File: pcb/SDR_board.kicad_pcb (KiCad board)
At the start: 4 copper layers, 100 x 100 mm, 469 parts, among them J1 USB_B_Mini, J201 Molex 73251-1150 SMA, J301 Molex 73251-1150 SMA, J401 Molex 73251-1150 SMA, J501 Molex 73251-1150 SMA, SW1 SW_Push, U1 AMS1117-3.3, U2 NB3L553, U201 BGA2803, U202 MSi001-Q40, U203 MAX19777AZA+, U204 ADS7883, U205 LMV712-N, U206 MAX19777AZA+, U207 ADS7883, U3 CY7C68013A-56PVX, U301 BGA2803, U302 MSi001-Q40, U303 MAX19777AZA+, U304 ADS7883, U305 LMV712-N, U306 MAX19777AZA+, U307 ADS7883, U401 BGA2803, U402 MSi001-Q40, U403 MAX19777AZA+, U404 ADS7883, U405 LMV712-N, U406 MAX19777AZA+, U407 ADS7883, U5 24LC128, U501 BGA2803, U502 MSi001-Q40, U503 MAX19777AZA+, U504 ADS7883, U505 LMV712-N, U506 MAX19777AZA+, U507 ADS7883, U6 MCP1825S, X1 XO32, X2 XO32

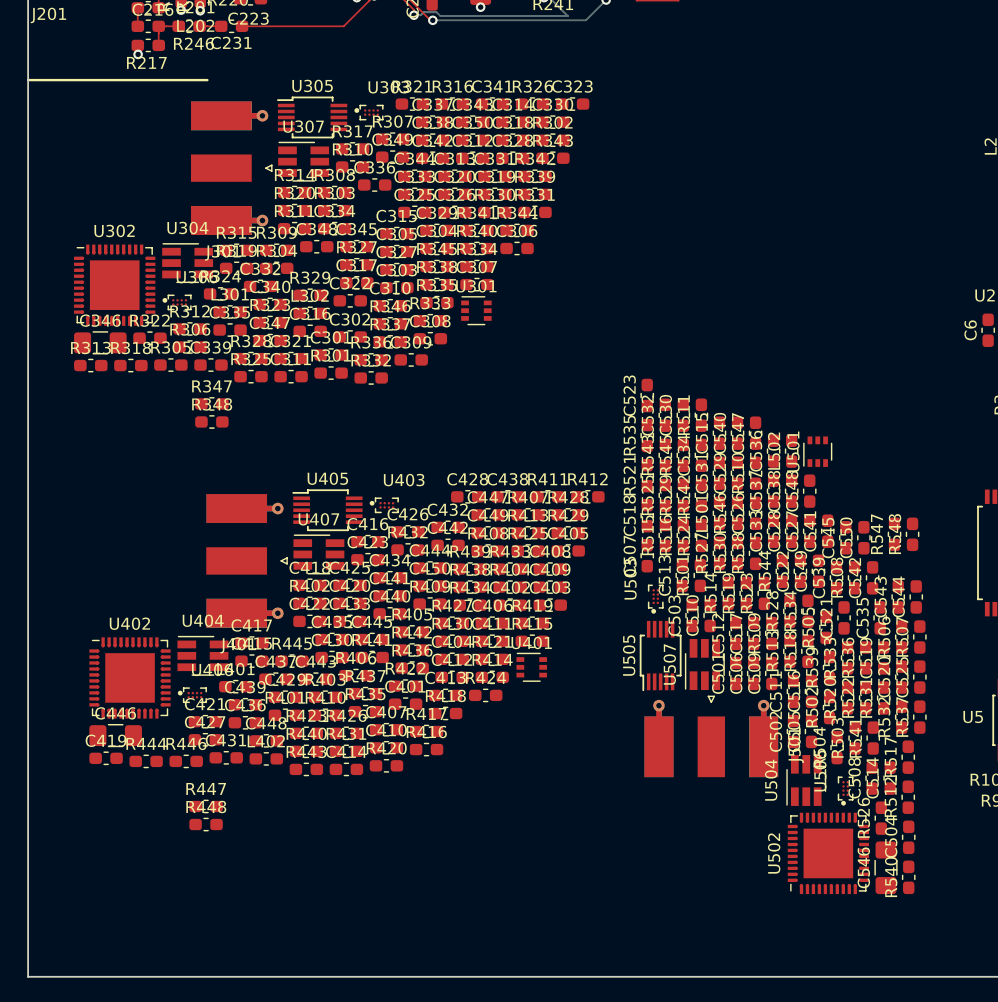
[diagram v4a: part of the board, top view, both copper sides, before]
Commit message: Duplicated the layouts for the other channels successfully using an old version of MitjaNemec/Kicad_action_plugins
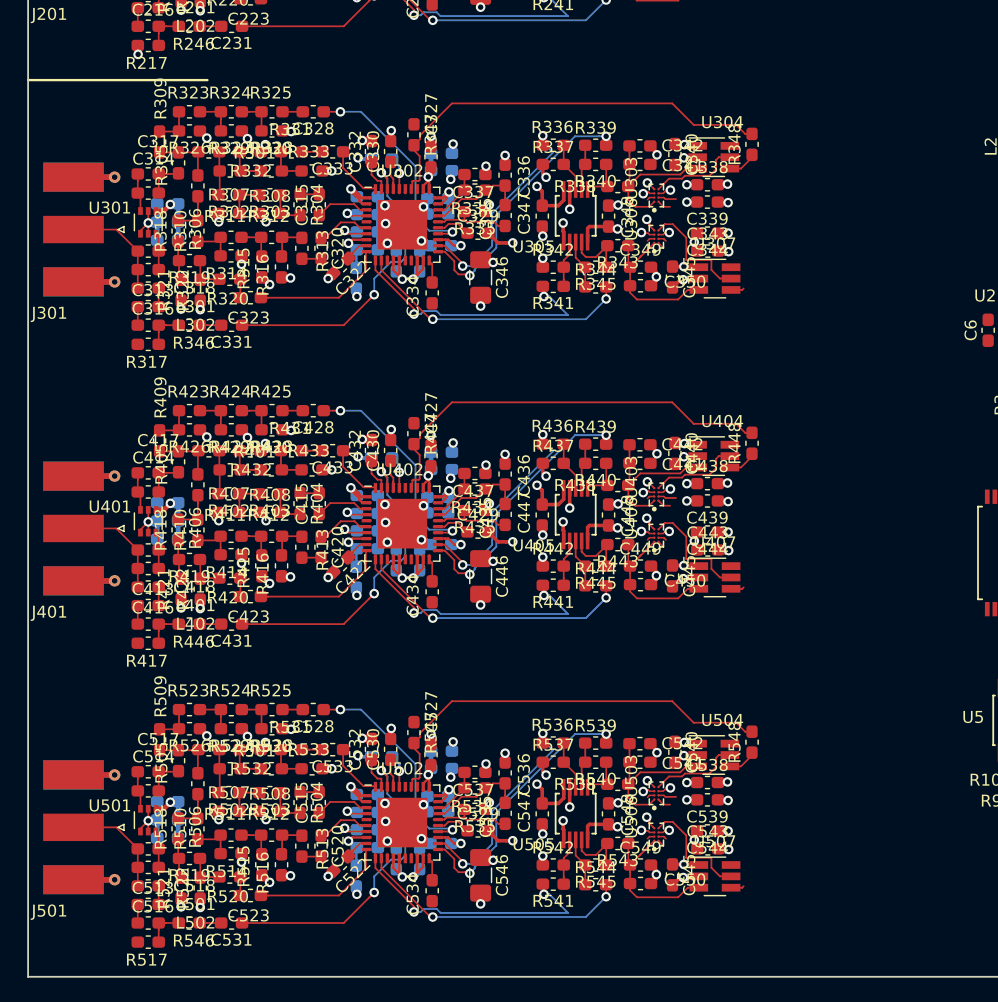
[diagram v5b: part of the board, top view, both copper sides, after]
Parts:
- C301, C302, C303, C304, C305, C306, C307, C308, C309, C310, C311, C312, C319, C321, C325, C326, C401, C402, C403, C404, C405, C406, C407, C408, C409, C410, C411, C412, C419, C421, C425, C426, C501, C502, C503, C504, C505, C506, C507, C508, C509, C510, C511, C512, C519, C521, C525, C526: moved to B.Cu
- moved L502 66.7 mm to (35.0, 115.5), turned to 0 degrees
- moved R517 65.4 mm to (35.0, 117.1), turned to 180 degrees
- moved U501 63.9 mm to (35.0, 106.9), turned to 270 degrees
- moved C514 62.1 mm to (35.0, 104.5), turned to 180 degrees
- moved R506 60.1 mm to (39.2, 103.8)
- moved R507 59.6 mm to (41.8, 106.2), turned to 0 degrees
- moved R526 58.3 mm to (38.5, 99.3), turned to 180 degrees
- moved L501 57.9 mm to (35.0, 114.0), turned to 180 degrees
- moved R522 57.9 mm to (39.4, 112.6)
- moved C516 57.4 mm to (35.0, 110.8), turned to 180 degrees
- moved R546 57.3 mm to (38.5, 115.5), turned to 180 degrees
- moved R448 55.7 mm to (85.5, 75.4), turned to 90 degrees
- moved C531 55.5 mm to (42.0, 115.5), turned to 180 degrees
- moved R510 55.3 mm to (39.2, 107.6)
- moved R505 55.3 mm to (37.6, 101.9), turned to 270 degrees
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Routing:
- net GND: track 80.2 -> 318.5 mm, vias 49 -> 193
- net +3.3VA: track 50.5 -> 201.8 mm, vias 19 -> 76
- net Net-(R547-Pad2): track 0.00 -> 35.3 mm
- net Net-(R447-Pad2): track 0.00 -> 35.3 mm
- net Net-(R347-Pad2): track 0.00 -> 35.3 mm
- net Net-(C331-Pad1): track 0.00 -> 26.4 mm, vias 0 -> 2
- net Net-(C531-Pad1): track 0.00 -> 26.4 mm, vias 0 -> 2
- net Net-(C431-Pad1): track 0.00 -> 26.4 mm, vias 0 -> 2
- net /Channel 4/I_N: track 0.00 -> 23.0 mm, vias 0 -> 2
- net /Channel 3/I_N: track 0.00 -> 23.0 mm, vias 0 -> 2
- net /Channel 2/I_N: track 0.00 -> 23.0 mm, vias 0 -> 2
- net /Channel 4/I_P: track 0.00 -> 22.4 mm, vias 0 -> 2
- net /Channel 3/I_P: track 0.00 -> 22.4 mm, vias 0 -> 2
- net /Channel 2/I_P: track 0.00 -> 22.4 mm, vias 0 -> 2
- net /Channel 4/Q_N: track 0.00 -> 21.8 mm, vias 0 -> 2
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
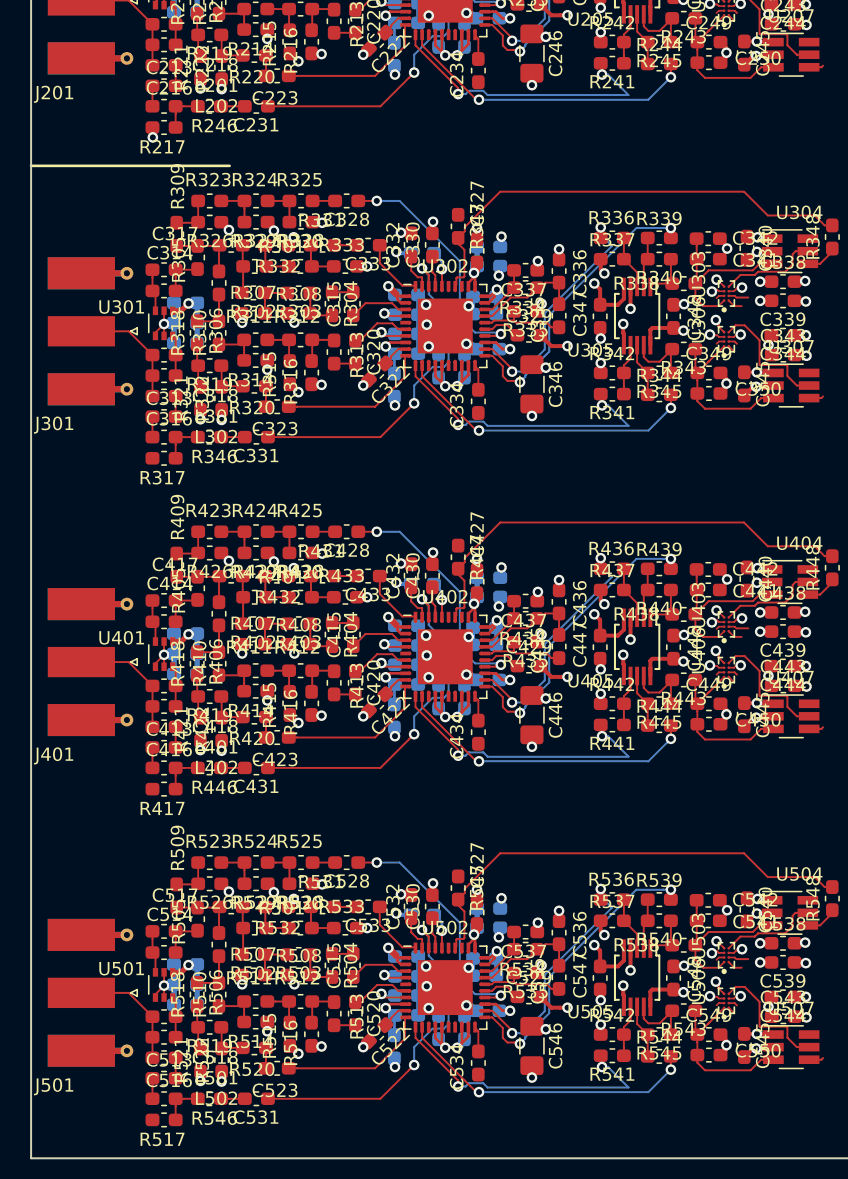
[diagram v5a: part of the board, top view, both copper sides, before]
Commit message: Stashing some possibly-breaking changes
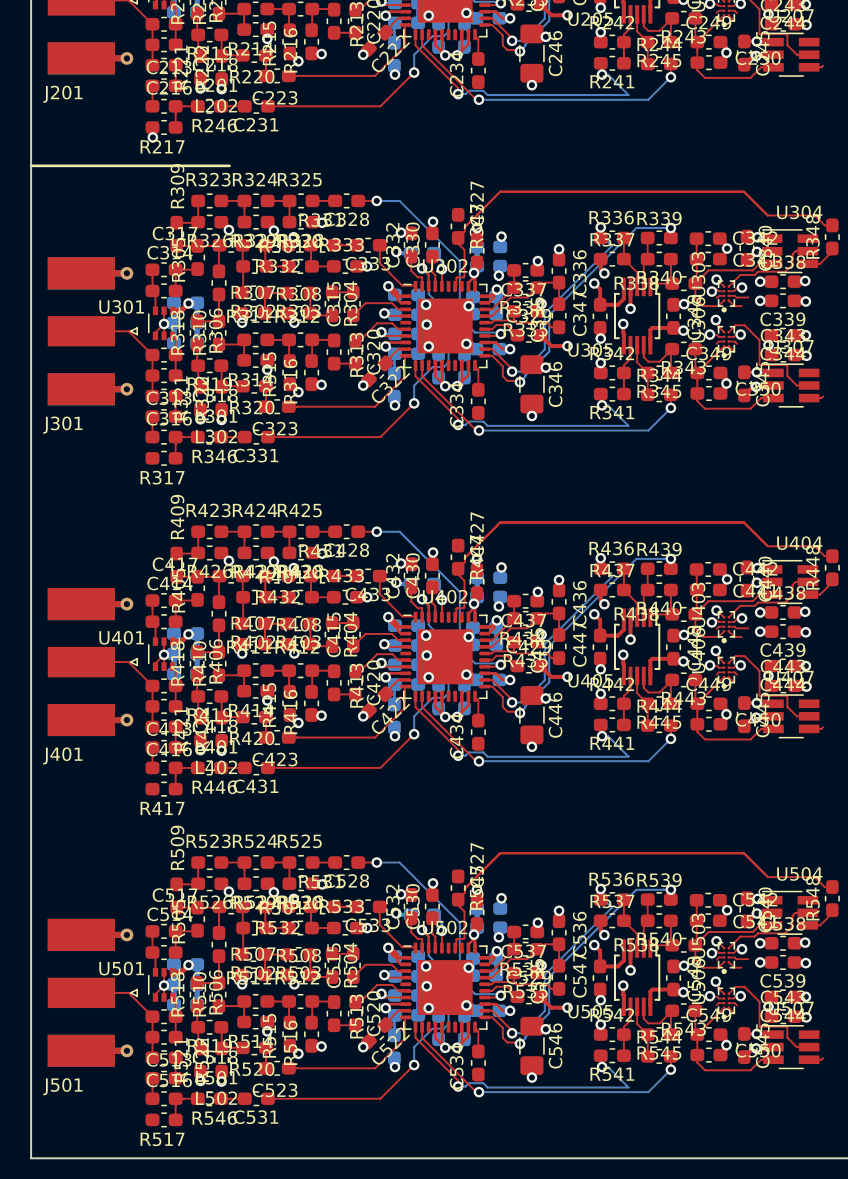
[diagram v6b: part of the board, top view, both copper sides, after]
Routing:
- net Net-(R547-Pad2): track 35.3 -> 60.1 mm
- net Net-(R447-Pad2): track 35.3 -> 60.1 mm
- net Net-(R347-Pad2): track 35.3 -> 60.1 mm
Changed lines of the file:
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@@
   (general
     (thickness 1.6)
-    (drawings 6)
-    (tracks 2558)
+    (drawings 5)
+    (tracks 2567)
     (zones 0)
     (modules 469)
@@
     (fp_line (start -1.65 -0.73) (end 1.65 -0.73) (layer F.CrtYd) (width 0.05))
     (fp_line (start -1.65 0.73) (end -1.65 -0.73) (layer F.CrtYd) (width 0.05))
-    (fp_line (start -0.171267 0.51) (end 0.171267 0.51) (layer F.SilkS) (width 0.12))
-    (fp_line (start -0.171267 -0.51) (end 0.171267 -0.51) (layer F.SilkS) (width 0.12))
+    (fp_line (start -0.171268 0.51) (end 0.171268 0.51) (layer F.SilkS) (width 0.12))
+    (fp_line (start -0.171268 -0.51) (end 0.171268 -0.51) (layer F.SilkS) (width 0.12))
     (fp_line (start 0.8 0.4) (end -0.8 0.4) (layer F.Fab) (width 0.1))
     (fp_line (start 0.8 -0.4) (end 0.8 0.4) (layer F.Fab) (width 0.1))
@@
     (fp_line (start 0.8 -0.4) (end 0.8 0.4) (layer F.Fab) (width 0.1))
     (fp_line (start 0.8 0.4) (end -0.8 0.4) (layer F.Fab) (width 0.1))
-    (fp_line (start -0.171267 -0.51) (end 0.171267 -0.51) (layer F.SilkS) (width 0.12))
-    (fp_line (start -0.171267 0.51) (end 0.171267 0.51) (layer F.SilkS) (width 0.12))
+    (fp_line (start -0.171268 -0.51) (end 0.171268 -0.51) (layer F.SilkS) (width 0.12))
+    (fp_line (start -0.171268 0.51) (end 0.171268 0.51) (layer F.SilkS) (width 0.12))
     (fp_line (start -1.65 0.73) (end -1.65 -0.73) (layer F.CrtYd) (width 0.05))
     (fp_line (start -1.65 -0.73) (end 1.65 -0.73) (layer F.CrtYd) (width 0.05))
@@
       (effects (font (size 0.4 0.4) (thickness 0.06)))
     )
-    (pad 1 smd roundrect (at -0.875 0 225) (size 1.05 0.95) (layers Front_1.Cu F.Paste F.Mask) (roundrect_rratio 0.25)
+    (pad 1 smd roundrect (at -0.874999 0 225) (size 1.05 0.95) (layers Front_1.Cu F.Paste F.Mask) (roundrect_rratio 0.25)
       (net 49 "Net-(C322-Pad1)"))
-    (pad 2 smd roundrect (at 0.875 0 225) (size 1.05 0.95) (layers Front_1.Cu F.Paste F.Mask) (roundrect_rratio 0.25)
+    (pad 2 smd roundrect (at 0.874999 0 225) (size 1.05 0.95) (layers Front_1.Cu F.Paste F.Mask) (roundrect_rratio 0.25)
       (net 2 GND))
     (model ${KISYS3DMOD}/Capacitor_SMD.3dshapes/C_0603_1608Metric.wrl
@@
     (fp_line (start 0.8 -0.4) (end 0.8 0.4) (layer F.Fab) (width 0.1))
     (fp_line (start 0.8 0.4) (end -0.8 0.4) (layer F.Fab) (width 0.1))
-    (fp_line (start -0.171267 -0.51) (end 0.171267 -0.51) (layer F.SilkS) (width 0.12))
-    (fp_line (start -0.171267 0.51) (end 0.171267 0.51) (layer F.SilkS) (width 0.12))
+    (fp_line (start -0.171268 -0.51) (end 0.171268 -0.51) (layer F.SilkS) (width 0.12))
+    (fp_line (start -0.171268 0.51) (end 0.171268 0.51) (layer F.SilkS) (width 0.12))
     (fp_line (start -1.65 0.73) (end -1.65 -0.73) (layer F.CrtYd) (width 0.05))
     (fp_line (start -1.65 -0.73) (end 1.65 -0.73) (layer F.CrtYd) (width 0.05))
@@
       (effects (font (size 0.4 0.4) (thickness 0.06)))
     )
-    (pad 1 smd roundrect (at -0.875 0 225) (size 1.05 0.95) (layers Front_1.Cu F.Paste F.Mask) (roundrect_rratio 0.25)
+    (pad 1 smd roundrect (at -0.874999 0 225) (size 1.05 0.95) (layers Front_1.Cu F.Paste F.Mask) (roundrect_rratio 0.25)
       (net 79 "Net-(C422-Pad1)"))
-    (pad 2 smd roundrect (at 0.875 0 225) (size 1.05 0.95) (layers Front_1.Cu F.Paste F.Mask) (roundrect_rratio 0.25)
+    (pad 2 smd roundrect (at 0.874999 0 225) (size 1.05 0.95) (layers Front_1.Cu F.Paste F.Mask) (roundrect_rratio 0.25)
       (net 2 GND))
     (model ${KISYS3DMOD}/Capacitor_SMD.3dshapes/C_0603_1608Metric.wrl
@@
     (fp_line (start -1.65 -0.73) (end 1.65 -0.73) (layer F.CrtYd) (width 0.05))
     (fp_line (start -1.65 0.73) (end -1.65 -0.73) (layer F.CrtYd) (width 0.05))
-    (fp_line (start -0.171267 0.51) (end 0.171267 0.51) (layer F.SilkS) (width 0.12))
-    (fp_line (start -0.171267 -0.51) (end 0.171267 -0.51) (layer F.SilkS) (width 0.12))
+    (fp_line (start -0.171268 0.51) (end 0.171268 0.51) (layer F.SilkS) (width 0.12))
+    (fp_line (start -0.171268 -0.51) (end 0.171268 -0.51) (layer F.SilkS) (width 0.12))
     (fp_line (start 0.8 0.4) (end -0.8 0.4) (layer F.Fab) (width 0.1))
     (fp_line (start 0.8 -0.4) (end 0.8 0.4) (layer F.Fab) (width 0.1))
     (fp_line (start -0.8 -0.4) (end 0.8 -0.4) (layer F.Fab) (width 0.1))
     (fp_line (start -0.8 0.4) (end -0.8 -0.4) (layer F.Fab) (width 0.1))
-    (pad 2 smd roundrect (at 0.875 0 225) (size 1.05 0.95) (layers Front_1.Cu F.Paste F.Mask) (roundrect_rratio 0.25)
+    (pad 2 smd roundrect (at 0.874999 0 225) (size 1.05 0.95) (layers Front_1.Cu F.Paste F.Mask) (roundrect_rratio 0.25)
       (net 2 GND))
-    (pad 1 smd roundrect (at -0.875 0 225) (size 1.05 0.95) (layers Front_1.Cu F.Paste F.Mask) (roundrect_rratio 0.25)
+    (pad 1 smd roundrect (at -0.874999 0 225) (size 1.05 0.95) (layers Front_1.Cu F.Paste F.Mask) (roundrect_rratio 0.25)
       (net 109 "Net-(C522-Pad1)"))
     (model ${KISYS3DMOD}/Capacitor_SMD.3dshapes/C_0603_1608Metric.wrl
@@
     (tags "sma edge")
     (attr smd)
-    (fp_text reference J201 (at -3.72 7) (layer F.SilkS)
+    (fp_text reference J201 (at -3.02 7) (layer F.SilkS)
       (effects (font (size 1 1) (thickness 0.15)))
     )
@@
     (tags "sma edge")
     (attr smd)
-    (fp_text reference J301 (at -3.72 7) (layer F.SilkS)
+    (fp_text reference J301 (at -3.02 7) (layer F.SilkS)
       (effects (font (size 1 1) (thickness 0.15)))
     )
@@
     (tags "sma edge")
     (attr smd)
-    (fp_text reference J401 (at -3.72 7) (layer F.SilkS)
+    (fp_text reference J401 (at -3.02 7) (layer F.SilkS)
       (effects (font (size 1 1) (thickness 0.15)))
     )
@@
     (tags "sma edge")
     (attr smd)
-    (fp_text reference J501 (at -3.72 7) (layer F.SilkS)
+    (fp_text reference J501 (at -3.02 7) (layer F.SilkS)
       (effects (font (size 1 1) (thickness 0.15)))
     )
@@
     )
   )
-  (gr_line (start 24 32.5) (end 21 32.5) (layer Dwgs.User) (width 0.2))
   (gr_line (start 25 45) (end 40 45) (layer F.SilkS) (width 0.2))
   (gr_line (start 25 120) (end 25 20) (layer Edge.Cuts) (width 0.15))
@@
   (segment (start 57.774072 24.950928) (end 57.774072 24.629294) (width 0.1468) (layer Front_1.Cu) (net 283))
   (segment (start 57.275 25.45) (end 57.774072 24.950928) (width 0.1468) (layer Front_1.Cu) (net 283))
-  (zone (net 2) (net_name GND) (layer Inner_2_GND.Cu) (hatch edge 0.508)
+  (segment (start 78.875 46.95) (end 80.675 48.75) (width 0.1468) (layer Front_1.Cu) (net 284))
+  (segment (start 60.453366 46.95) (end 78.875 46.95) (width 0.1468) (layer Front_1.Cu) (net 284))
+  (segment (start 57.774072 49.629294) (end 60.453366 46.95) (width 0.1468) (layer Front_1.Cu) (net 284))
+  (segment (start 78.875 71.95) (end 80.675 73.75) (width 0.1468) (layer Front_1.Cu) (net 285))
+  (segment (start 60.453366 71.95) (end 78.875 71.95) (width 0.1468) (layer Front_1.Cu) (net 285))
+  (segment (start 57.774072 74.629294) (end 60.453366 71.95) (width 0.1468) (layer Front_1.Cu) (net 285))
+  (segment (start 78.875 96.95) (end 80.675 98.75) (width 0.1468) (layer Front_1.Cu) (net 286))
+  (segment (start 60.453366 96.95) (end 78.875 96.95) (width 0.1468) (layer Front_1.Cu) (net 286))
+  (segment (start 57.774072 99.629294) (end 60.453366 96.95) (width 0.1468) (layer Front_1.Cu) (net 286))
+  (zone (net 1) (net_name +3V3) (layer Inner_3_PWR.Cu) (hatch edge 0.508)
     (connect_pads (clearance 0.3))
     (min_thickness 0.254)
@@
     (polygon
       (pts
-        (xy 24.6 19.25) (xy 125.8 19.35) (xy 126.35 121.4) (xy 23.2 121.1)
+        (xy 94.912243 18.953362) (xy 127.825 18.875) (xy 128.375 120.925) (xy 93.512243 120.803362)
       )
     )
@@
     )
   )
-  (zone (net 1) (net_name +3V3) (layer Inner_3_PWR.Cu) (hatch edge 0.508)
+  (zone (net 2) (net_name GND) (layer Inner_2_GND.Cu) (hatch edge 0.508)
     (connect_pads (clearance 0.3))
     (min_thickness 0.254)
@@
     (polygon
       (pts
-        (xy 94.912243 18.953362) (xy 127.825 18.875) (xy 128.375 120.925) (xy 93.512243 120.803362)
+        (xy 24.6 19.25) (xy 125.8 19.35) (xy 126.35 121.4) (xy 23.2 121.1)
       )
     )

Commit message: stashing some layout changes
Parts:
- moved J1 13.5 mm to (121.8, 70.0)
- moved D1 12.2 mm to (110.3, 100.8)
- moved D2 12.2 mm to (110.3, 97.0)
- moved R7 12.2 mm to (113.9, 97.0)
- moved R8 12.2 mm to (113.9, 100.8)
- moved C13 7.82 mm to (100.8, 94.2)
- moved C15 7.70 mm to (105.5, 73.3)
- moved C22 7.70 mm to (110.3, 73.2)
- moved C6 7.70 mm to (97.8, 67.7)
- moved C8 7.70 mm to (105.3, 68.7)
- moved C9 7.70 mm to (110.3, 67.9)
- moved R3 7.70 mm to (100.3, 73.9)
- moved R4 7.70 mm to (102.3, 73.9)
- moved R5 7.70 mm to (107.8, 65.3)
- moved U2 7.70 mm to (101.5, 67.8)
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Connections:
- net Net-(J1-Pad2) renamed /D_N
- net Net-(J1-Pad3) renamed /D_P
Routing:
- net /D_P: track 0.00 -> 30.1 mm
- net /D_N: track 0.00 -> 30.0 mm
- net /TUNER_1_CLK: track 0.00 -> 28.4 mm
- net /Channel 1/Q_P: track 18.7 -> 21.7 mm
- net /Channel 1/Q_N: track 21.8 -> 22.6 mm
